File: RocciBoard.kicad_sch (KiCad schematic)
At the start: 203 parts, among them J1 Battery, J10 M3, J11 I2C6, J12 Power, J13 M2, J14 I2C7, J2 I2C0, J3 I2C1, J4 I2C2, J5 I2C3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

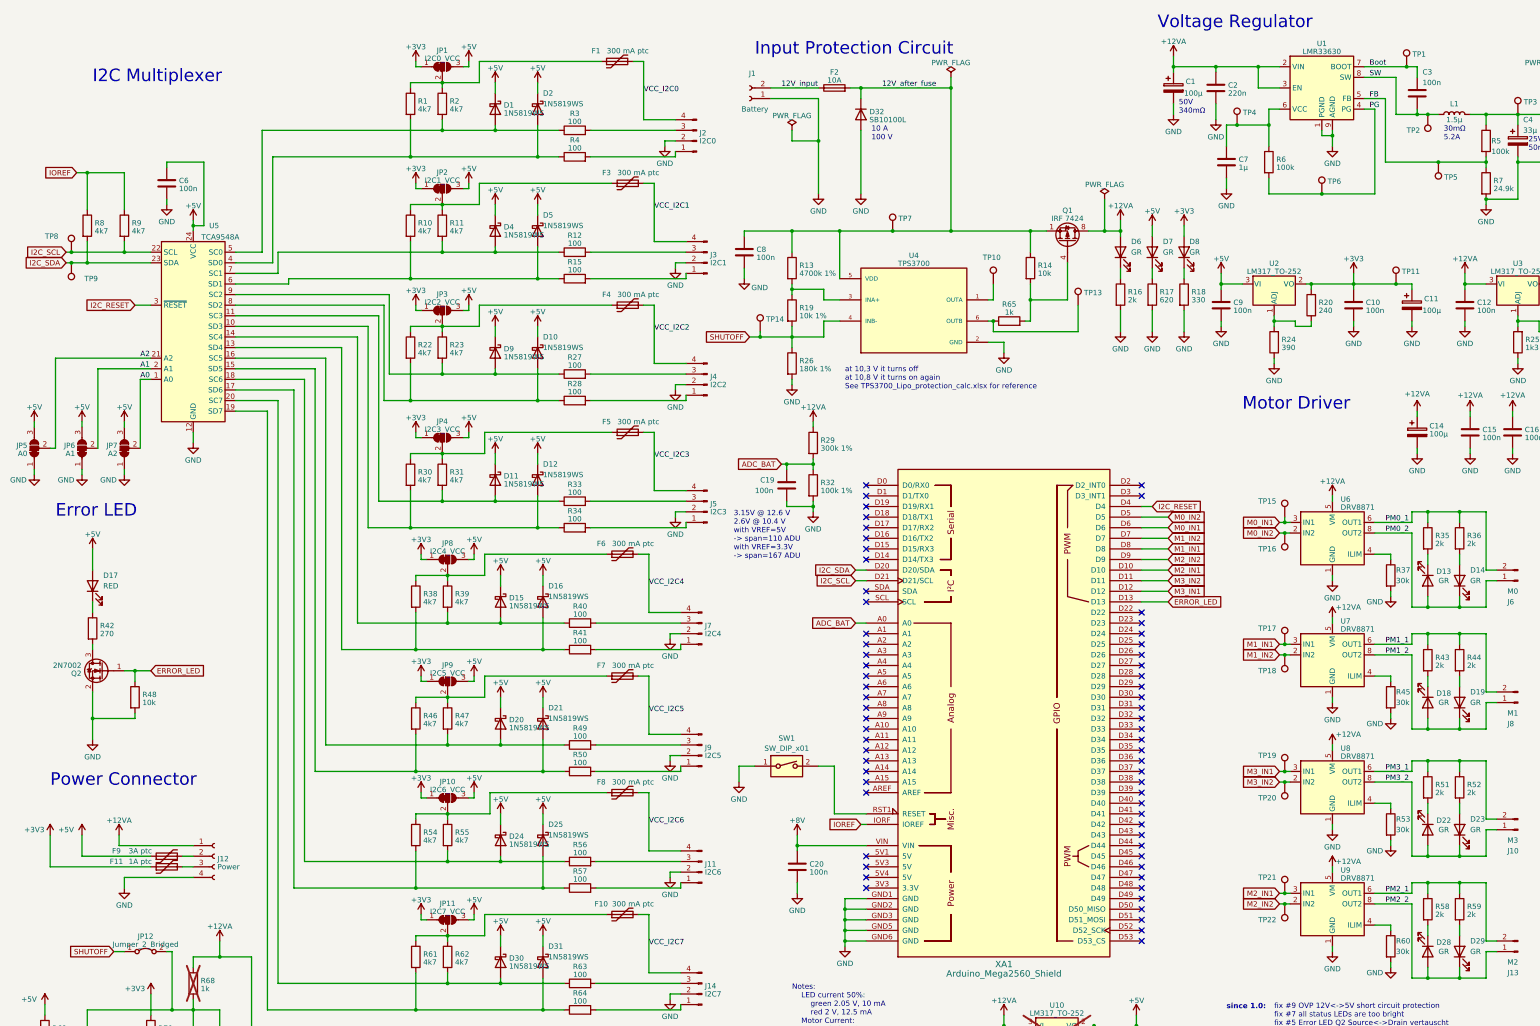
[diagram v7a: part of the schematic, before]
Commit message: added 2S lipo support to the schematic
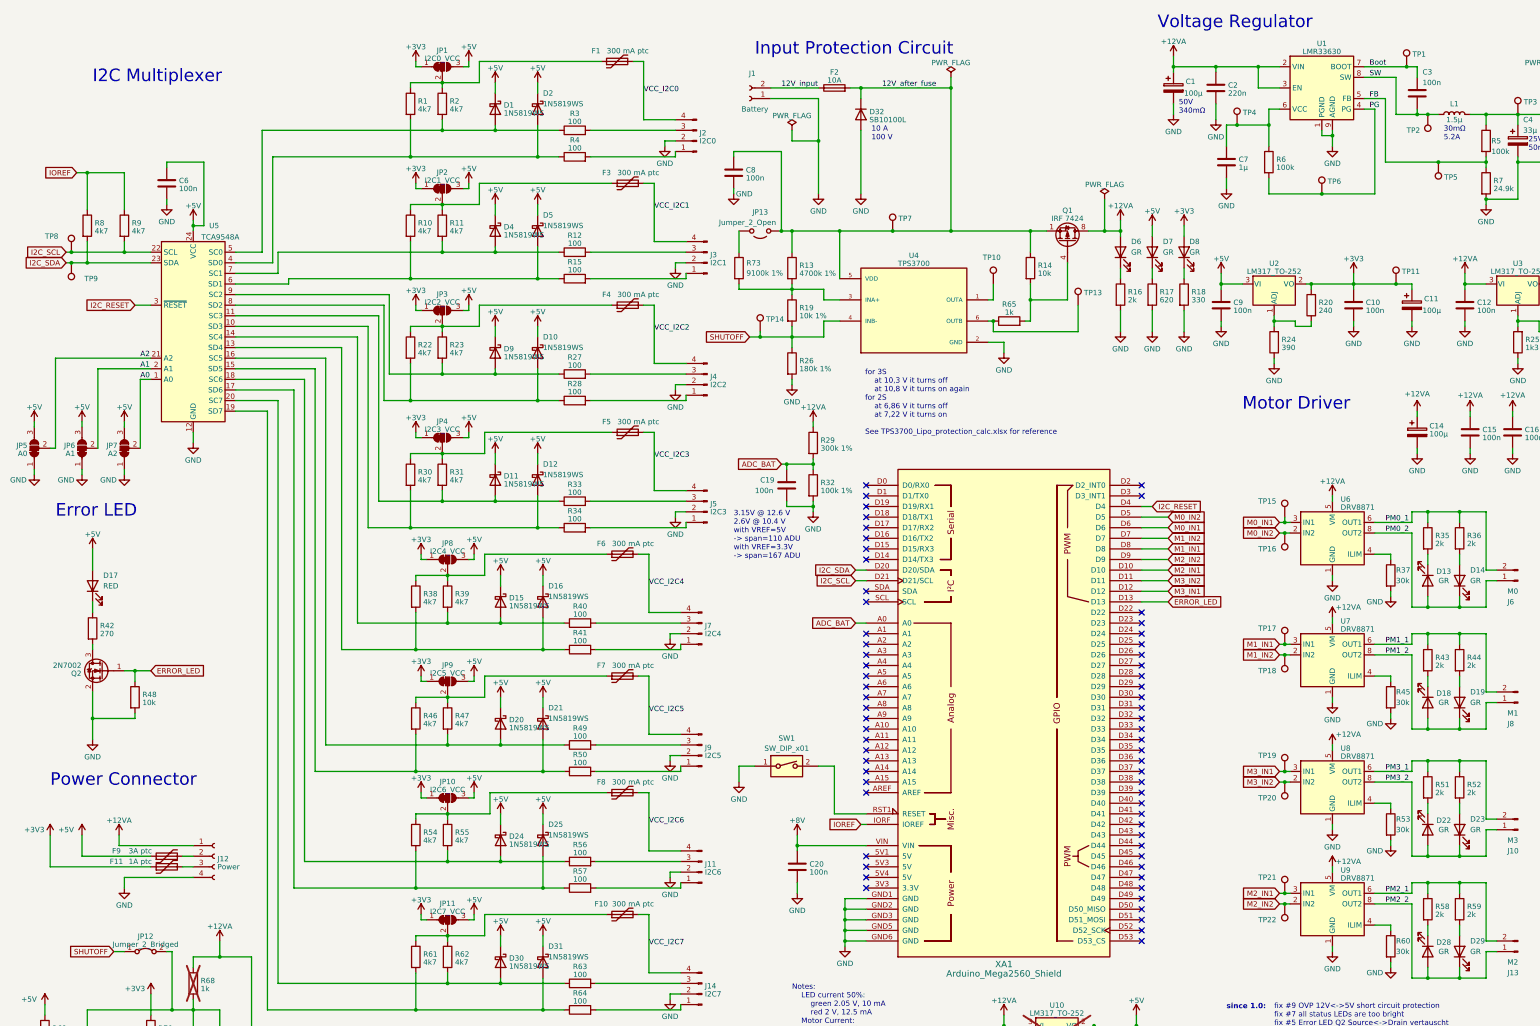
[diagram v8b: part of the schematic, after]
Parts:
- added JP13: Jumper_2_Open, symbol Jumper:Jumper_2_Open
- added R73: 9100k 1%, Resistor_SMD:R_0603_1608Metric, symbol Device:R
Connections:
- net 12V_after_fuse: now also JP13.1 (A)
- net at R13.2, R19.1, U4.3 (INA+): now also R73.2
- new net: JP13.2 (B), R73.1
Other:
- note added: "for 3S at 10,3 V it turns off at 10,8 V it turns on again for 2S at 6,86 V it turns off at 7,22 V it turns on See TPS3700_Lipo_protection_calc.xlsx for reference"
- note removed: "at 10,3 V it turns off at 10,8 V it turns on again See TPS3700_Lipo_protection_calc.xlsx for reference"
- moved on the sheet: C8
